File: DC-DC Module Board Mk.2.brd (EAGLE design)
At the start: 177.9 x 101.7 mm, 159 parts, among them Q1 FDN340P, U2 AP1117_LIN_REG, U3 LM1085IS-5.0

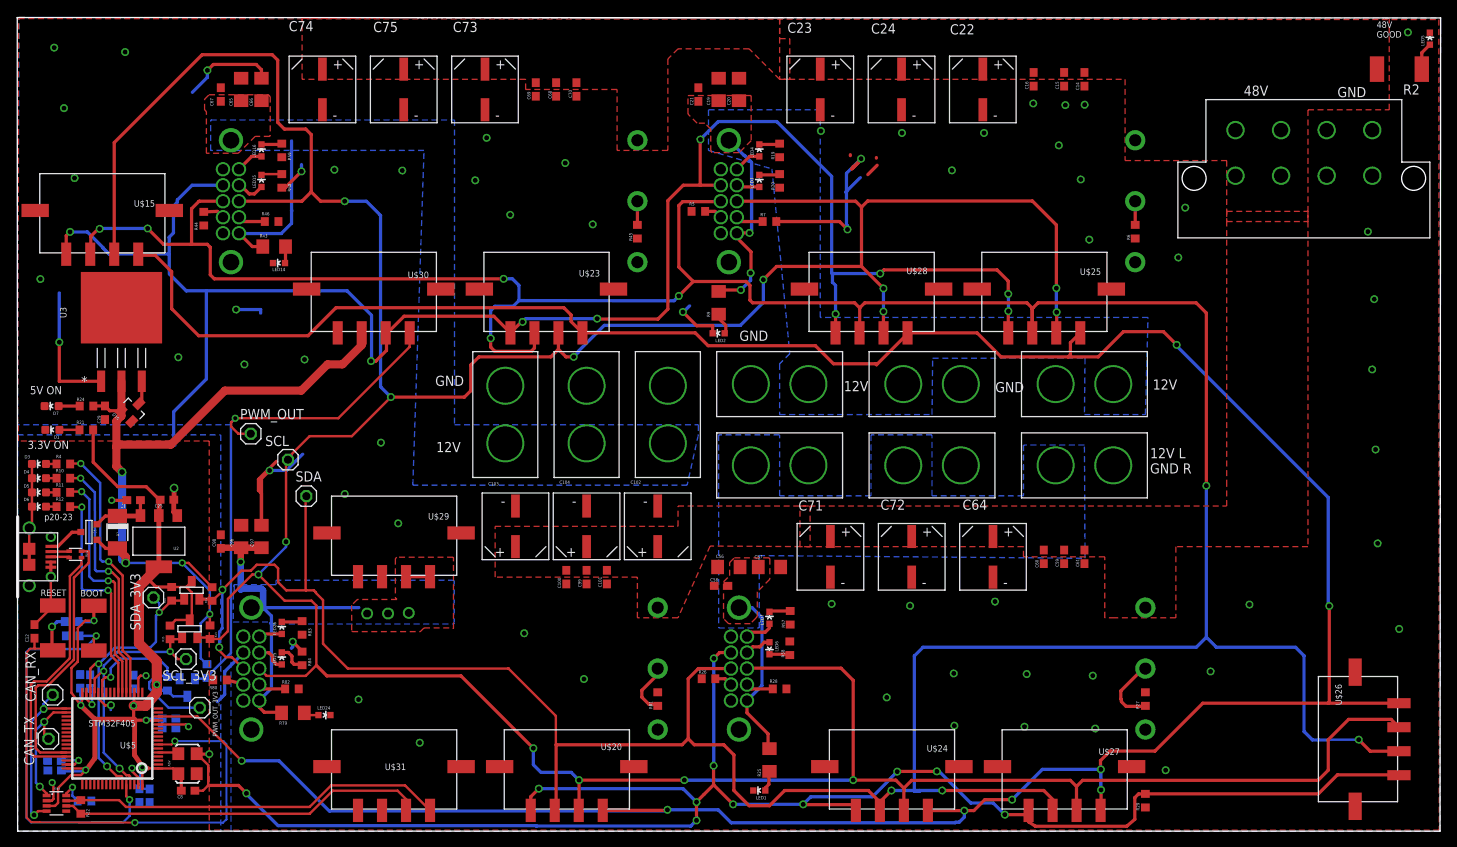
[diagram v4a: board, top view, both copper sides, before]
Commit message: added screws, moved led in top right (power), assured drc rules
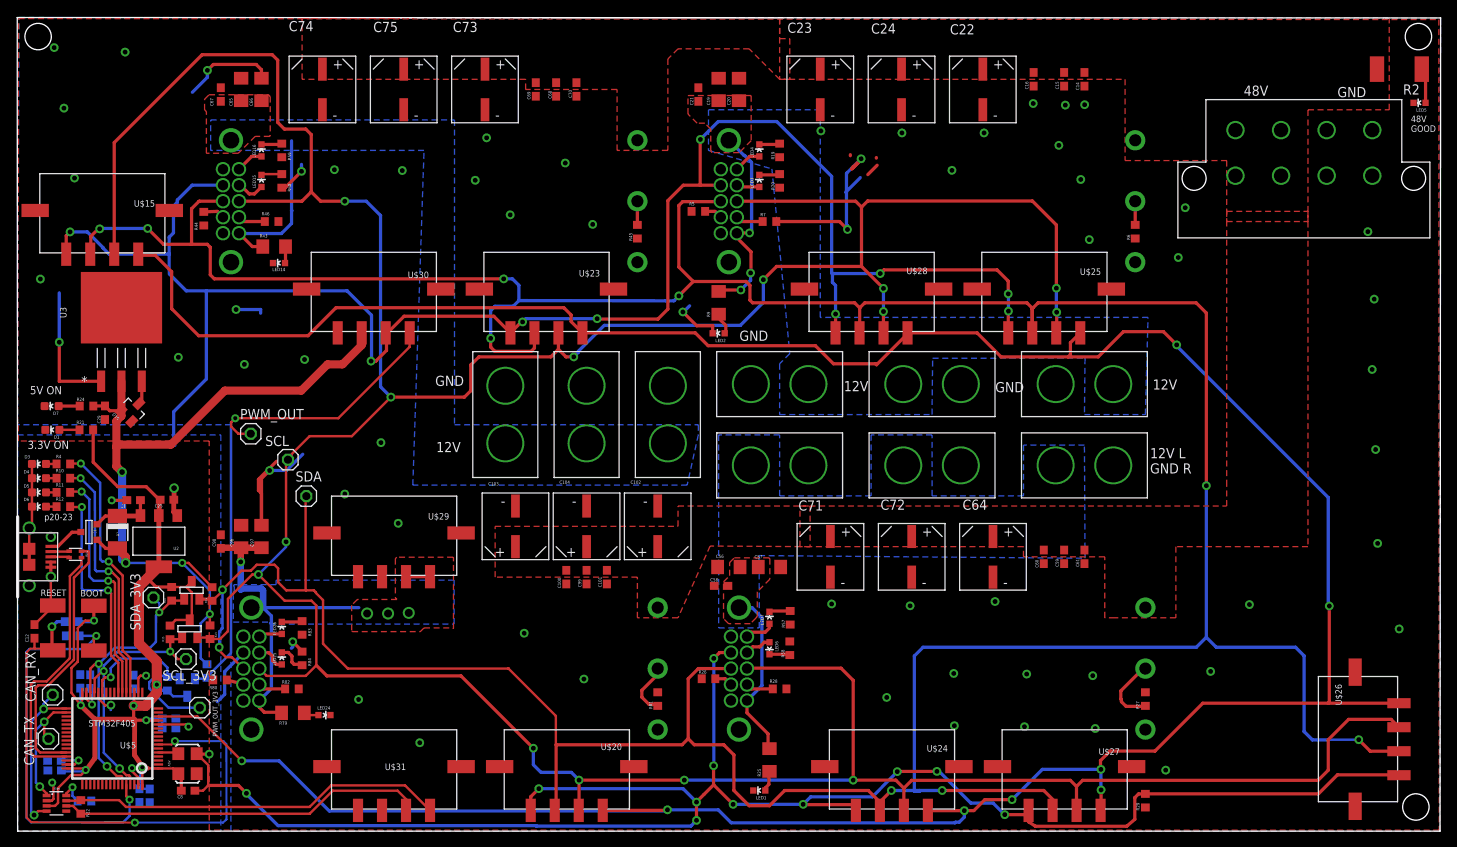
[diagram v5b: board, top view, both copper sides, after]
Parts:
- added U$32, U$33, U$7: (no value), SparkFun-Electromechanical:STAND-OFF
- moved LED5 8.12 mm to (175.2, 89.8), turned to 90 degrees
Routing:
- net N$2: track 3.48 -> 4.40 mm
- net GND: vias 62 -> 61
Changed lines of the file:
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@@
 <text x="1.2446" y="46.5074" size="1.016" layer="25">3.3V ON</text>
 <text x="3.3274" y="37.592" size="0.8128" layer="25">p20-23</text>
-<text x="169.8676" y="97.9186" size="0.8128" layer="25">48V
+<text x="174.1576" y="86.1386" size="0.8128" layer="25">48V
 GOOD</text>
 <text x="52.324" y="46.101" size="1.27" layer="25">12V</text>
@@
 <param name="rlMinPadBottom" value="10mil"/>
 <param name="rlMaxPadBottom" value="20mil"/>
-<param name="rlMinViaOuter" value="8mil"/>
+<param name="rlMinViaOuter" value="10mil"/>
 <param name="rlMaxViaOuter" value="20mil"/>
-<param name="rlMinViaInner" value="8mil"/>
+<param name="rlMinViaInner" value="10mil"/>
 <param name="rlMaxViaInner" value="20mil"/>
 <param name="rlMinMicroViaOuter" value="4mil"/>
@@
 </element>
 <element name="U$13" library="Connectors" package="MEGA-FIT-8" value="MEGA-FIT-8" x="176.53" y="90.17" rot="R180"/>
-<element name="LED5" library="SparkFun" package="LED-0603" value="GREEN" x="176.53" y="97.79">
-<attribute name="PARTNO" value="160-1446-1-ND" x="171.45" y="109.22" size="1.778" layer="27" display="off"/>
-<attribute name="BOM" value="INCLUDE" x="171.45" y="109.22" size="1.778" layer="27" display="off"/>
+<element name="LED5" library="SparkFun" package="LED-0603" value="GREEN" x="175.24" y="89.77" rot="R90">
+<attribute name="PARTNO" value="160-1446-1-ND" x="163.81" y="84.69" size="1.778" layer="27" rot="R90" display="off"/>
+<attribute name="BOM" value="INCLUDE" x="163.81" y="84.69" size="1.778" layer="27" rot="R90" display="off"/>
 </element>
 <element name="R2" library="resistor" package="R2512" value="2700" x="172.72" y="93.98" rot="R180">
@@
 <attribute name="PROD_ID" value="DIO-00819" x="4.34" y="48.89" size="1.778" layer="27" rot="R90" display="off"/>
 </element>
+<element name="U$7" library="SparkFun-Electromechanical" package="STAND-OFF" value="" x="2.56" y="98.05"/>
+<element name="U$32" library="SparkFun-Electromechanical" package="STAND-OFF" value="" x="175.1" y="98.05"/>
+<element name="U$33" library="SparkFun-Electromechanical" package="STAND-OFF" value="" x="174.78" y="1.75"/>
 </elements>
 <signals>
@@
 <via x="169.5704" y="65.2272" extent="1-16" drill="0.6"/>
 <via x="168.783" y="73.66" extent="1-16" drill="0.6"/>
-<via x="173.7868" y="98.5774" extent="1-16" drill="0.6"/>
 <wire x1="107.442" y1="81.9658" x2="106.2736" y2="80.7974" width="0.4064" layer="1"/>
 <wire x1="104.0892" y1="83.2866" x2="104.0892" y2="83.1596" width="0.4064" layer="1"/>
@@
 <contactref element="R2" pad="1"/>
 <contactref element="LED5" pad="A"/>
-<wire x1="175.52" y1="93.98" x2="175.52" y2="96.03" width="0.4064" layer="1"/>
-<wire x1="175.52" y1="96.03" x2="176.53" y2="97.04" width="0.4064" layer="1"/>
+<wire x1="175.52" y1="93.98" x2="175.99" y2="93.51" width="0.4064" layer="1"/>
+<wire x1="175.99" y1="93.51" x2="175.99" y2="89.77" width="0.4064" layer="1"/>
 </signal>
 <signal name="N$22">

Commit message: redoing fixes/re-adding bypass capacitor on can
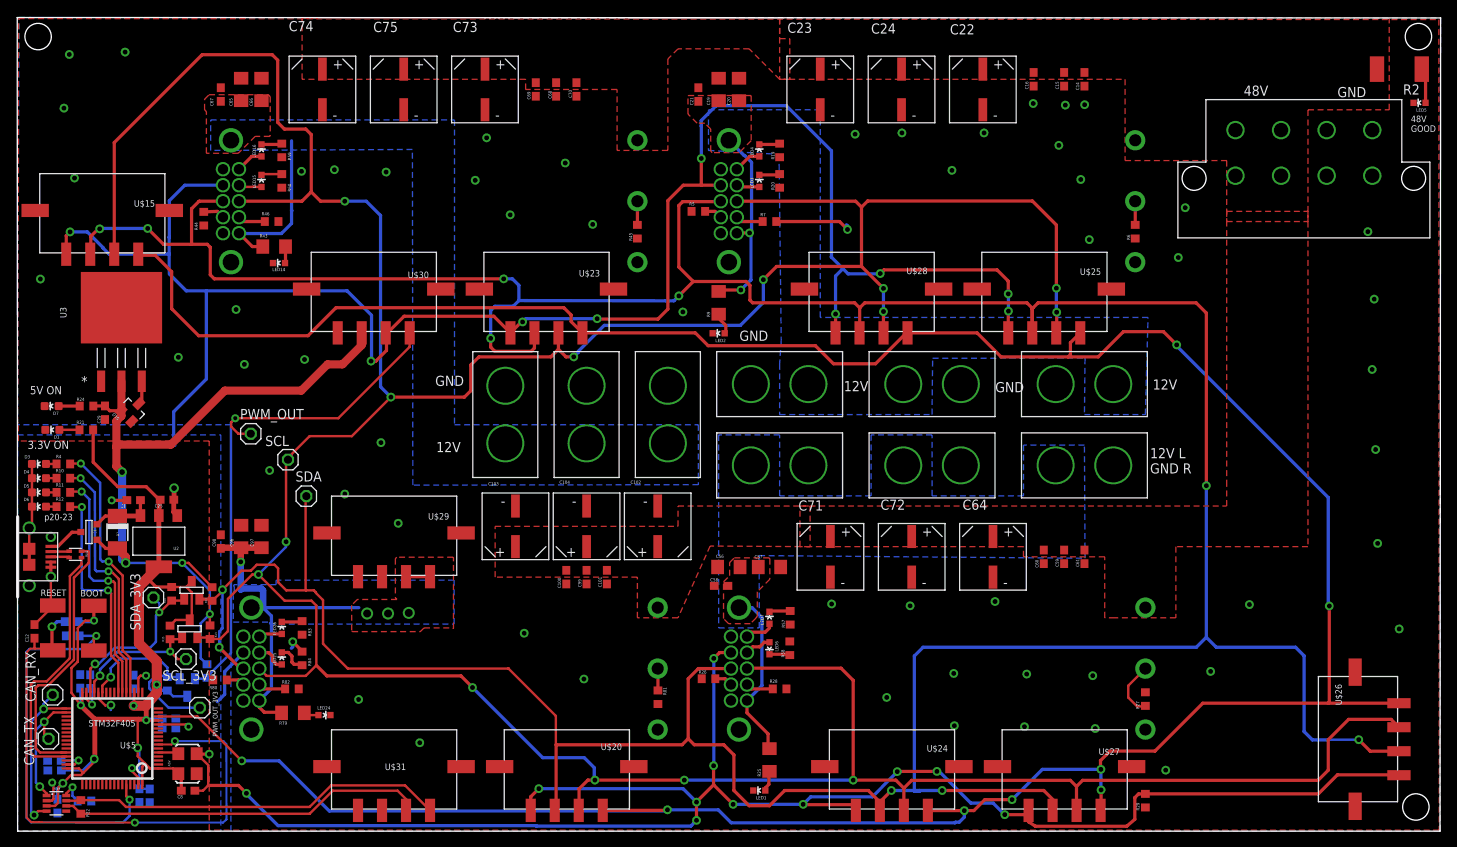
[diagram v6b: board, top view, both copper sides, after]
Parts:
- added C13: 0.1uF, rcl:C0603
- moved R81 0.23 mm to (80.0, 15.5), turned to 90 degrees
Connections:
- net +3V3: now also C13.1
- net DGND: now also C13.2
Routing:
- net GND: track 93.4 -> 12.6 mm, vias 61 -> 58
- net SDA1: track 38.1 -> 22.4 mm, vias 3 -> 2
- net SCL1: track 33.4 -> 18.5 mm, vias 3 -> 2
- net +3V3: track 142.9 -> 148.3 mm, vias 7 -> 8
- net DGND: track 499.1 -> 504.1 mm
- net N$44: track 6.83 -> 2.74 mm
- net N$8: track 8.87 -> 7.13 mm
- net SCL: track 504.1 -> 504.8 mm
- net PG2: track 3.62 -> 2.90 mm
- net +12V1: track 26.1 -> 25.8 mm, vias 3 -> 2
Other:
- board text removed: "SCL test"
- board text removed: "SDA test"
